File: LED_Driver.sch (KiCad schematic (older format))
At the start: 6 parts, among them U7 AP5726

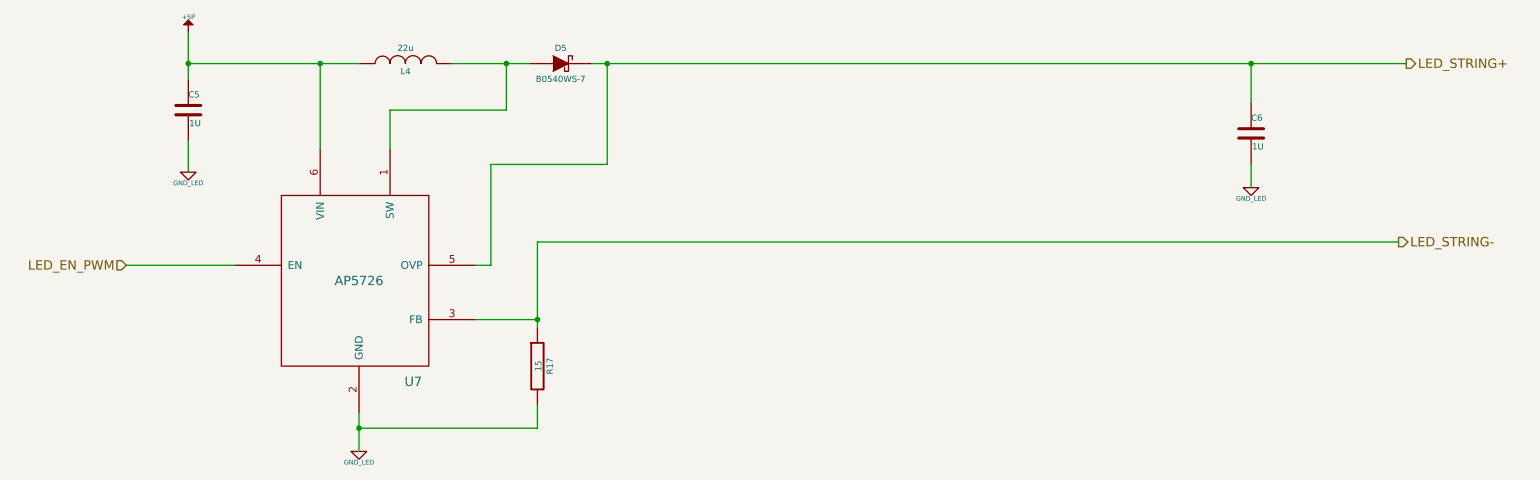
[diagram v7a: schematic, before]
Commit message: Added the schematic and BOM changes back in after hard reset
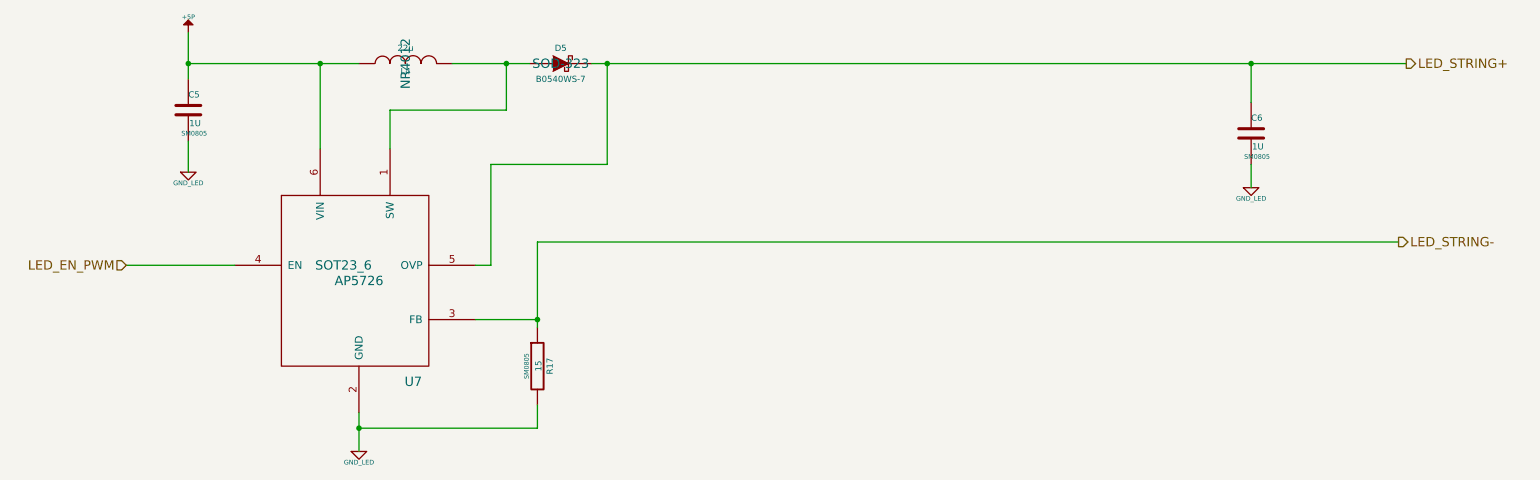
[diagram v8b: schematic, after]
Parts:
- C5, C6, R17: footprint ~ -> SM0805
- D5: footprint ~ -> SOD-323
- L4: footprint ~ -> NR4012
- U7: footprint (none) -> SOT23_6
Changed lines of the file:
@@
-EESchema Schematic File Version 2  date 4/16/2014 11:04:06 PM
+EESchema Schematic File Version 2  date 4/18/2014 9:49:53 PM
 LIBS:power
 LIBS:device
@@
 Sheet 3 9
 Title ""
-Date "17 apr 2014"
+Date "19 apr 2014"
 Rev ""
 Comp ""
@@
 F 0 "U7" H 4000 2400 60  0000 C CNN
 F 1 "AP5726" H 3650 3050 60  0000 C CNN
-F 2 "" H 3550 3150 60  0000 C CNN
+F 2 "SOT23_6" H 3550 3150 60  0000 C CNN
 F 3 "" H 3550 3150 60  0000 C CNN
 	1    3650 3050
@@
 F 0 "C5" H 2550 2050 40  0000 L CNN
 F 1 "1U" H 2556 1865 40  0000 L CNN
-F 2 "~" H 2588 1800 30  0000 C CNN
+F 2 "SM0805" H 2588 1800 30  0000 C CNN
 F 3 "~" H 2550 1950 60  0000 C CNN
 	1    2550 1950
@@
 F 0 "C6" H 9400 2200 40  0000 L CNN
 F 1 "1U" H 9406 2015 40  0000 L CNN
-F 2 "~" H 9438 1950 30  0000 C CNN
+F 2 "SM0805" H 9438 1950 30  0000 C CNN
 F 3 "~" H 9400 2100 60  0000 C CNN
 	1    9400 2100
@@
 F 0 "L4" V 3900 1650 40  0000 C CNN
 F 1 "22u" V 4050 1650 40  0000 C CNN
-F 2 "~" H 3950 1650 60  0000 C CNN
+F 2 "NR4012" H 3950 1650 60  0000 C CNN
 F 3 "~" H 3950 1650 60  0000 C CNN
 F 4 "NR4012T220M" H 3950 1650 60  0001 C CNN "MFG Part Number"
@@
 F 0 "D5" H 4950 1750 40  0000 C CNN
 F 1 "B0540WS-7" H 4950 1550 40  0000 C CNN
-F 2 "~" H 4950 1650 60  0000 C CNN
+F 2 "SOD-323" H 4950 1650 60  0000 C CNN
 F 3 "~" H 4950 1650 60  0000 C CNN
 	1    4950 1650
@@
 F 0 "R17" V 4880 3600 40  0000 C CNN
 F 1 "15" V 4807 3601 40  0000 C CNN
-F 2 "~" V 4730 3600 30  0000 C CNN
+F 2 "SM0805" V 4730 3600 30  0000 C CNN
 F 3 "~" H 4800 3600 30  0000 C CNN
 	1    4800 3600
